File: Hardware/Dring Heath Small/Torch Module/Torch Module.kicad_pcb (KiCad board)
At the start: 2 copper layers, 124 x 68.5 mm, 75 parts, among them J1 Torch, J10 Module conn, J11 Conn_01x18_Male, J12 Conn_01x02_Male, J14 Conn_01x02_Male, J15 Module conn, J2 Module3, J3 Conn_01x18_Male, J4 Limit, J6 Motor, J7 Module1, J8 Torch, J9 2.54 pin, K1 G6E, Q1 IRLML2402, Q2 IRLML2402, Q3 IRLML2402, Q4 IRLML2402, Q5 IRLML2402, U1 ULN2002, U2 NCV8114ASN150T1G, U3 ADS1115IDGS

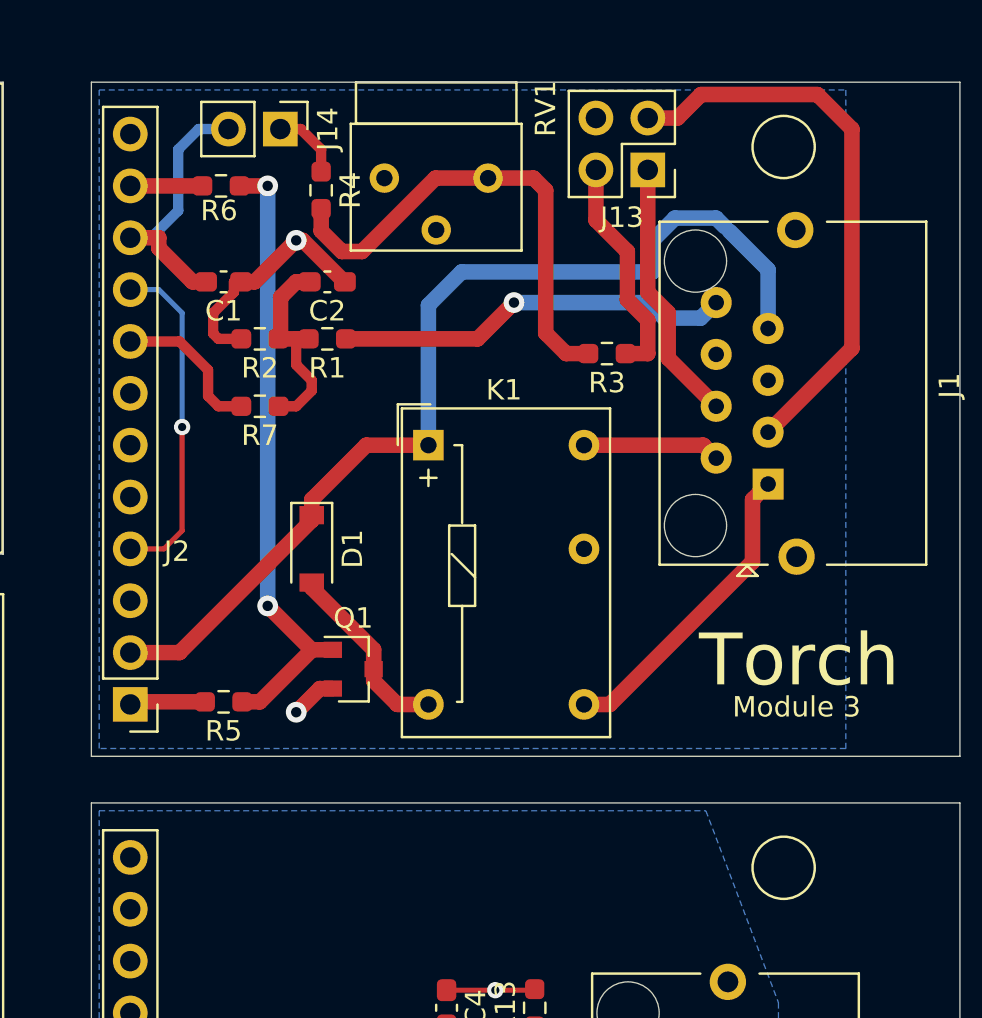
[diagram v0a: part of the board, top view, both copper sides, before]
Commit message: Torch1Module.sch alternate A/D input
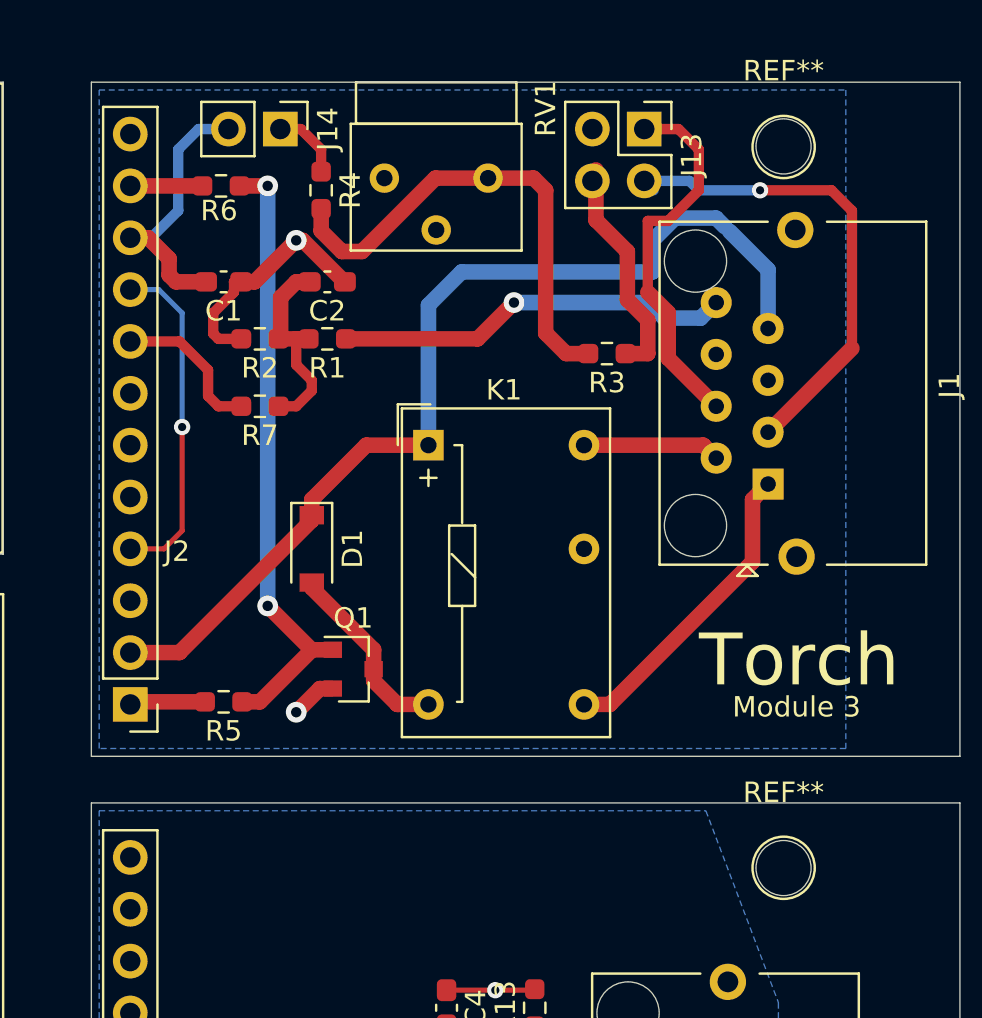
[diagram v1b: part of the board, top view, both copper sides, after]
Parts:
- added REF**: MountingHole_2.7mm_M2.5, MountingHole:MountingHole_2.7mm_M2.5, F.Cu at (152.7, 91.2)
- added REF**: MountingHole_2.7mm_M2.5, MountingHole:MountingHole_2.7mm_M2.5, F.Cu at (152.7, 55.9)
- moved J13 2.01 mm to (145.8, 55.0), turned to 270 degrees
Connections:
- C1 pad 2: Net-(C1-Pad2) -> Net-(J14-Pad2)
- J13 pad 2: Net-(J13-Pad2) -> Net-(J1-Pad3)
- J13 pad 3: Net-(J1-Pad3) -> Net-(C1-Pad1)
- J13 pad 4: Net-(C1-Pad1) -> Net-(J13-Pad4)
- R3 pad 1: Net-(J13-Pad2) -> Net-(J13-Pad4)
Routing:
- net Net-(J13-Pad4): track 0.00 -> 11.1 mm
- net Net-(J13-Pad2): track 11.1 -> 0.00 mm
- net Net-(J1-Pad4): track 13.0 -> 18.7 mm
- net Net-(J14-Pad2): track 8.77 -> 13.8 mm
- net Net-(C1-Pad2): track 8.40 -> 3.50 mm
- net Net-(J1-Pad3): track 27.7 -> 24.0 mm, vias 0 -> 1

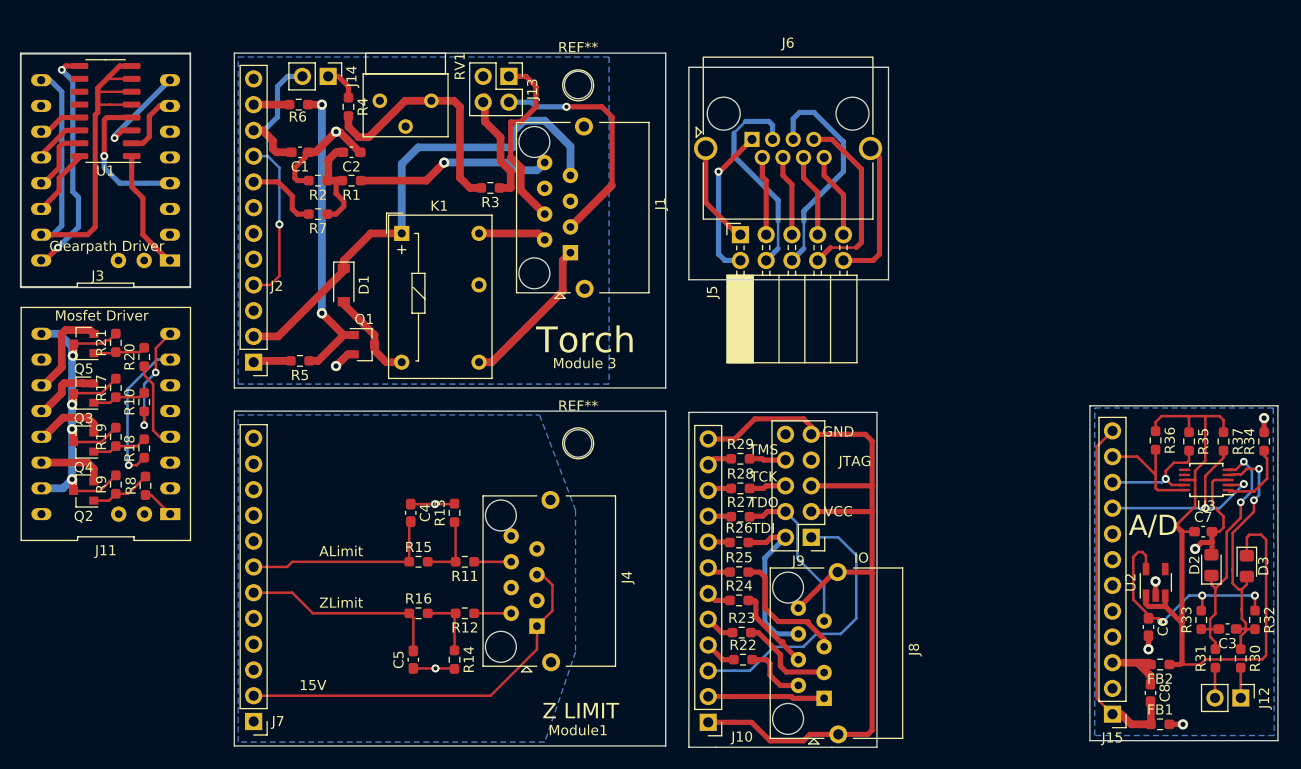
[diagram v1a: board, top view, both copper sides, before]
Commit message: Modified clamped A/D input updates panalized boards
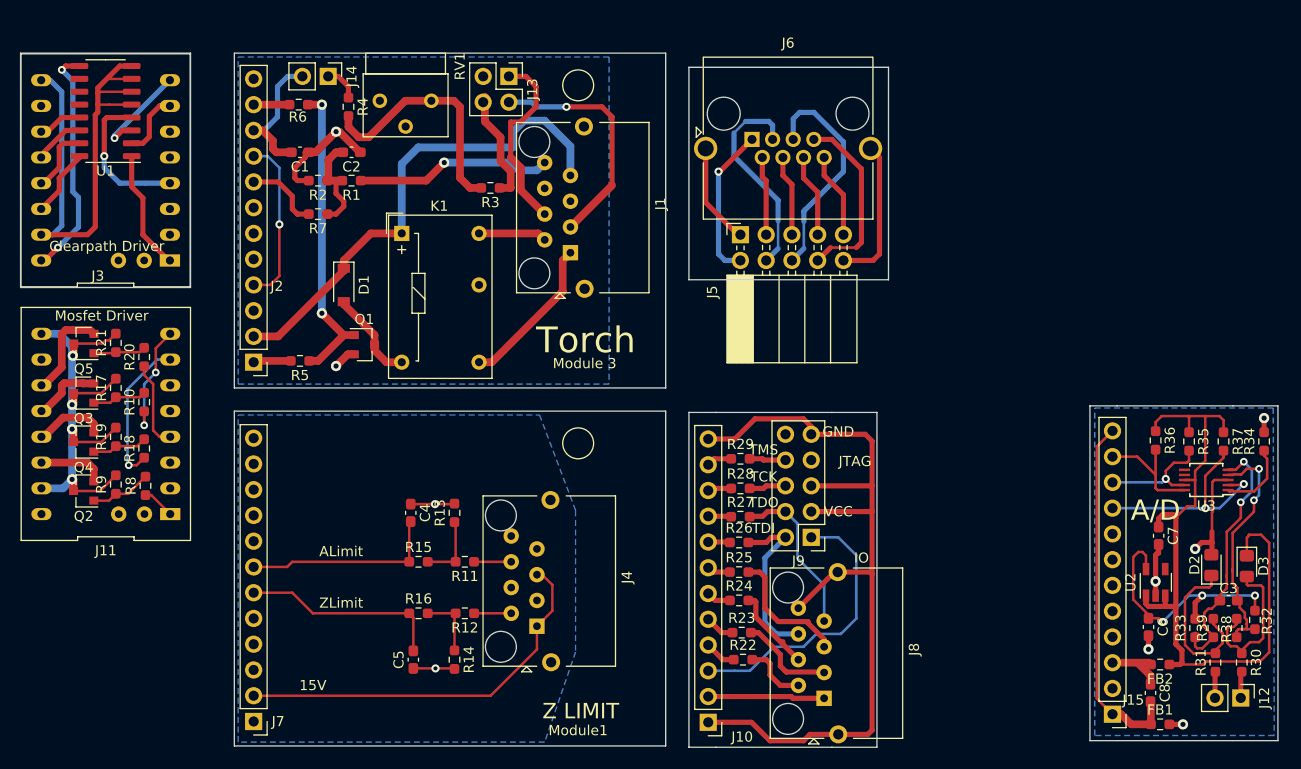
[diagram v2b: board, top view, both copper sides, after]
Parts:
- removed REF** (x2): MountingHole_2.7mm_M2.5, MountingHole:MountingHole_2.7mm_M2.5
- added R38: 200, Resistor_SMD:R_0603_1608Metric_Pad0.98x0.95mm_HandSolder, F.Cu at (217.6, 109.4)
- added R39: 200, Resistor_SMD:R_0603_1608Metric_Pad0.98x0.95mm_HandSolder, F.Cu at (215.3, 109.4)
- C3: value 100nf -> 22nf
- D2, D3: value D_Schottky_Small -> MSCD104H
- R31: value 1k -> 2k
- moved C7 4.42 mm to (209.9, 100.3), turned to 270 degrees
- moved C3 2.80 mm to (216.8, 106.7)
- moved R33 1.00 mm to (213.5, 109.4)
- moved R30 0.41 mm to (218.1, 112.8)
- moved R31 0.40 mm to (215.5, 112.8)
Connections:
- C1 pad 2: Net-(J14-Pad2) -> Net-(C1-Pad2)
- D2 pad 1: Net-(C3-Pad2) -> Net-(D2-Pad1)
- D3 pad 2: Net-(C3-Pad1) -> Net-(D3-Pad2)
- R30 pad 1: Net-(C3-Pad1) -> Net-(D3-Pad2)
- R31 pad 2: Net-(C3-Pad2) -> Net-(D2-Pad1)
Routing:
- net Net-(D2-Pad1): track 0.00 -> 16.2 mm
- net Net-(D3-Pad2): track 0.00 -> 15.4 mm
- net Net-(C3-Pad1): track 26.7 -> 24.0 mm
- net Net-(C6-Pad2): track 17.6 -> 20.1 mm
- net Net-(C7-Pad1): track 70.6 -> 71.8 mm
- net Net-(C6-Pad1): track 24.3 -> 25.4 mm

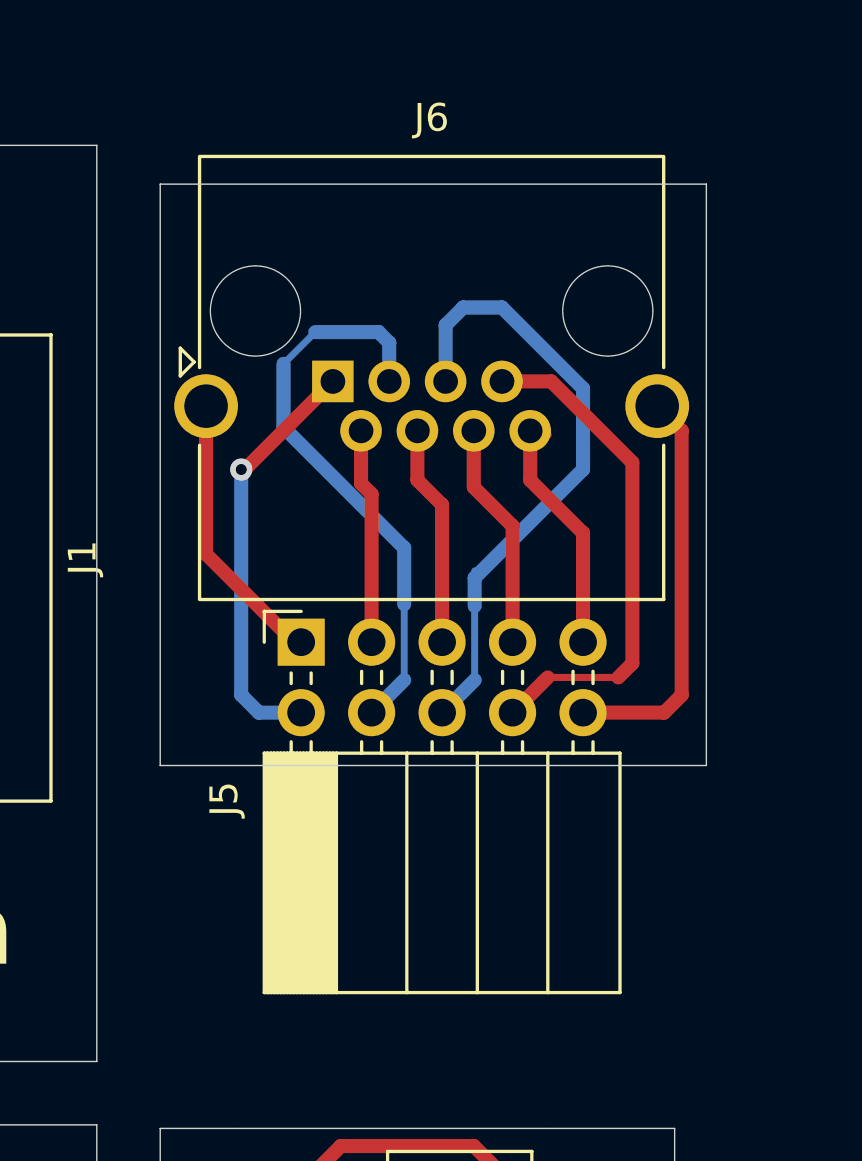
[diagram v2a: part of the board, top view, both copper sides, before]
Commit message: Changed RJ45 conector on motor driver module
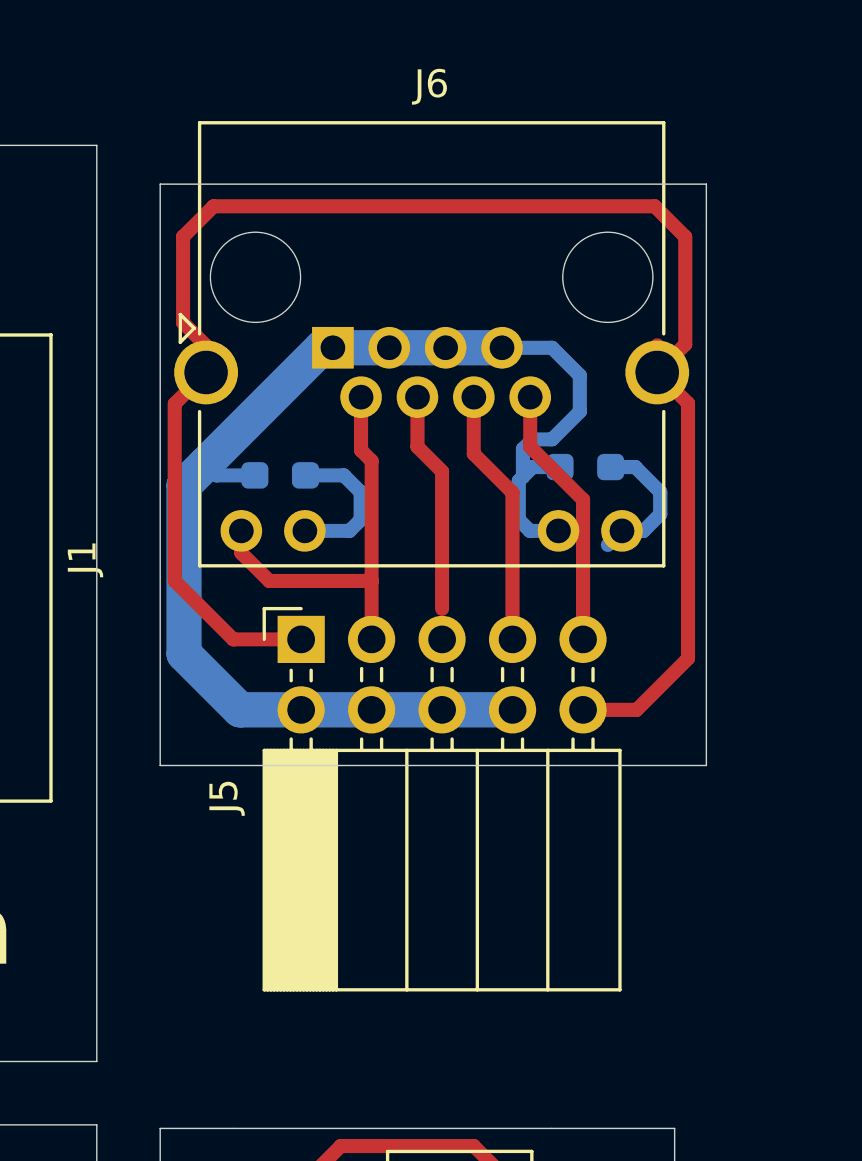
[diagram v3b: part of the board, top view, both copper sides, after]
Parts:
- added R40: 1k, Resistor_SMD:R_0603_1608Metric_Pad0.98x0.95mm_HandSolder, B.Cu at (178.9, 64.3)
- added R41: 1k, Resistor_SMD:R_0603_1608Metric_Pad0.98x0.95mm_HandSolder, B.Cu at (167.9, 64.6)
- J6: value Motor -> 8P8C_LED_Shielded; footprint Connector_RJ:RJ45_Amphenol_RJHSE5380 -> Connector_RJ:RJ45_Amphenol_RJHSE538X
- moved J6 1.21 mm to (169.8, 60.0)
- moved J5 0.10 mm to (168.7, 70.5)
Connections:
- J5 pad 10: Net-(J5-Pad10) -> Net-(J5-Pad1)
- J5 pad 4: Net-(J5-Pad4) -> Net-(J5-Pad2)
- J5 pad 6: Net-(J5-Pad6) -> Net-(J5-Pad2)
- J5 pad 8: Net-(J5-Pad8) -> Net-(J5-Pad2)
- J6 pad 10: Net-(J5-Pad10) -> Net-(J6-Pad10)
- J6 pad 3: Net-(J5-Pad4) -> Net-(J5-Pad2)
- J6 pad 5: Net-(J5-Pad6) -> Net-(J5-Pad2)
- J6 pad 7: Net-(J5-Pad8) -> Net-(J5-Pad2)
- J6 pad 9: Net-(J5-Pad1) -> Net-(J5-Pad3)
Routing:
- net Net-(J5-Pad1): track 10.1 -> 59.5 mm
- net Net-(J5-Pad2): track 15.2 -> 47.0 mm, vias 1 -> 0
- net Net-(J5-Pad6): track 23.5 -> 0.00 mm
- net Net-(J5-Pad4): track 22.5 -> 0.00 mm
- net Net-(J5-Pad8): track 18.6 -> 0.00 mm
- net Net-(J5-Pad10): track 14.6 -> 0.00 mm
- net Net-(J5-Pad3): track 8.28 -> 14.8 mm
- net Net-(J6-Pad12): track 0.00 -> 5.88 mm
- net Net-(J6-Pad10): track 0.00 -> 5.44 mm
- net Net-(J5-Pad7): track 8.49 -> 9.59 mm

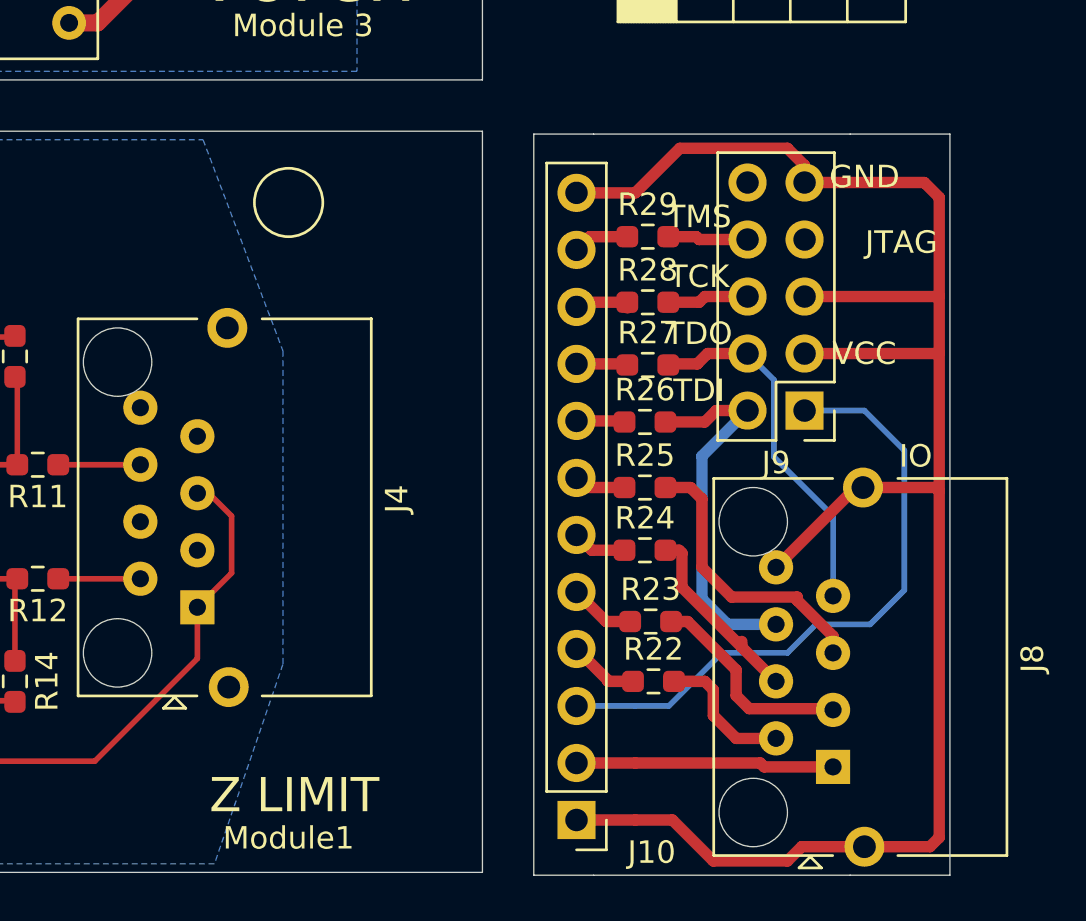
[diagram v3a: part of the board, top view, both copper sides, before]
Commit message: Updated torch module boards for external reset
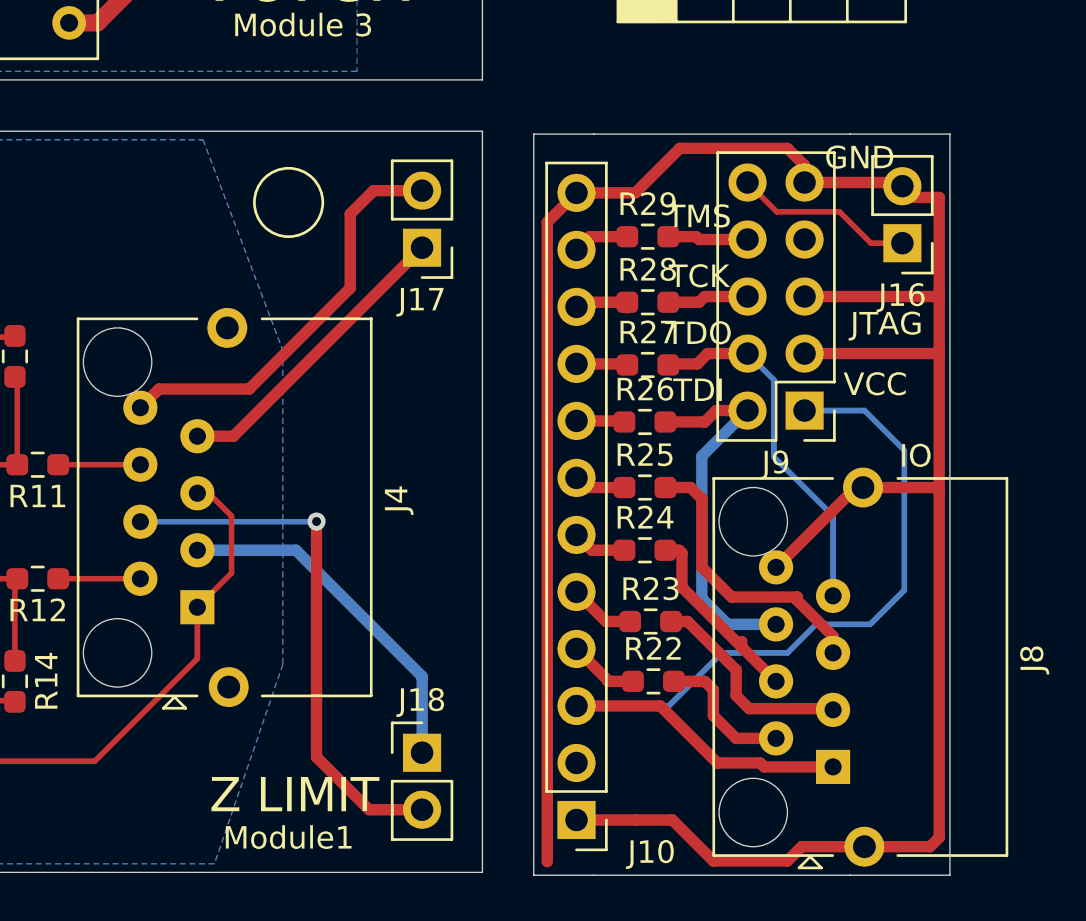
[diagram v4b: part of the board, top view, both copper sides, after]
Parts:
- added J16: Reset, Connector_PinHeader_2.54mm:PinHeader_1x02_P2.54mm_Vertical, F.Cu at (180.0, 93.0)
- added J17: Reset, Connector_PinHeader_2.54mm:PinHeader_1x02_P2.54mm_Vertical, F.Cu at (158.6, 93.2)
- added J18: Reset, Connector_PinHeader_2.54mm:PinHeader_1x02_P2.54mm_Vertical, F.Cu at (158.6, 115.7)
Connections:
- J5 pad 10: Net-(J5-Pad1) -> Net-(J5-Pad10)
- J8 pad 1: Net-(J10-Pad2) -> Net-(J10-Pad3)
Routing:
- net Net-(J10-Pad1): track 85.0 -> 115.4 mm
- net Net-(J18-Pad2): track 0.00 -> 24.0 mm, vias 0 -> 1
- net Net-(J17-Pad2): track 0.00 -> 18.5 mm
- net Net-(J18-Pad1): track 0.00 -> 15.7 mm
- net Net-(J17-Pad1): track 0.00 -> 13.5 mm
- net Net-(J10-Pad3): track 28.1 -> 40.7 mm
- net Net-(J10-Pad2): track 11.5 -> 0.00 mm
- net Net-(J16-Pad1): track 0.00 -> 8.02 mm
